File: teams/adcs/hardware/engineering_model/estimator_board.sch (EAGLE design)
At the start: 58 parts, among them U1 Value, U2 Value

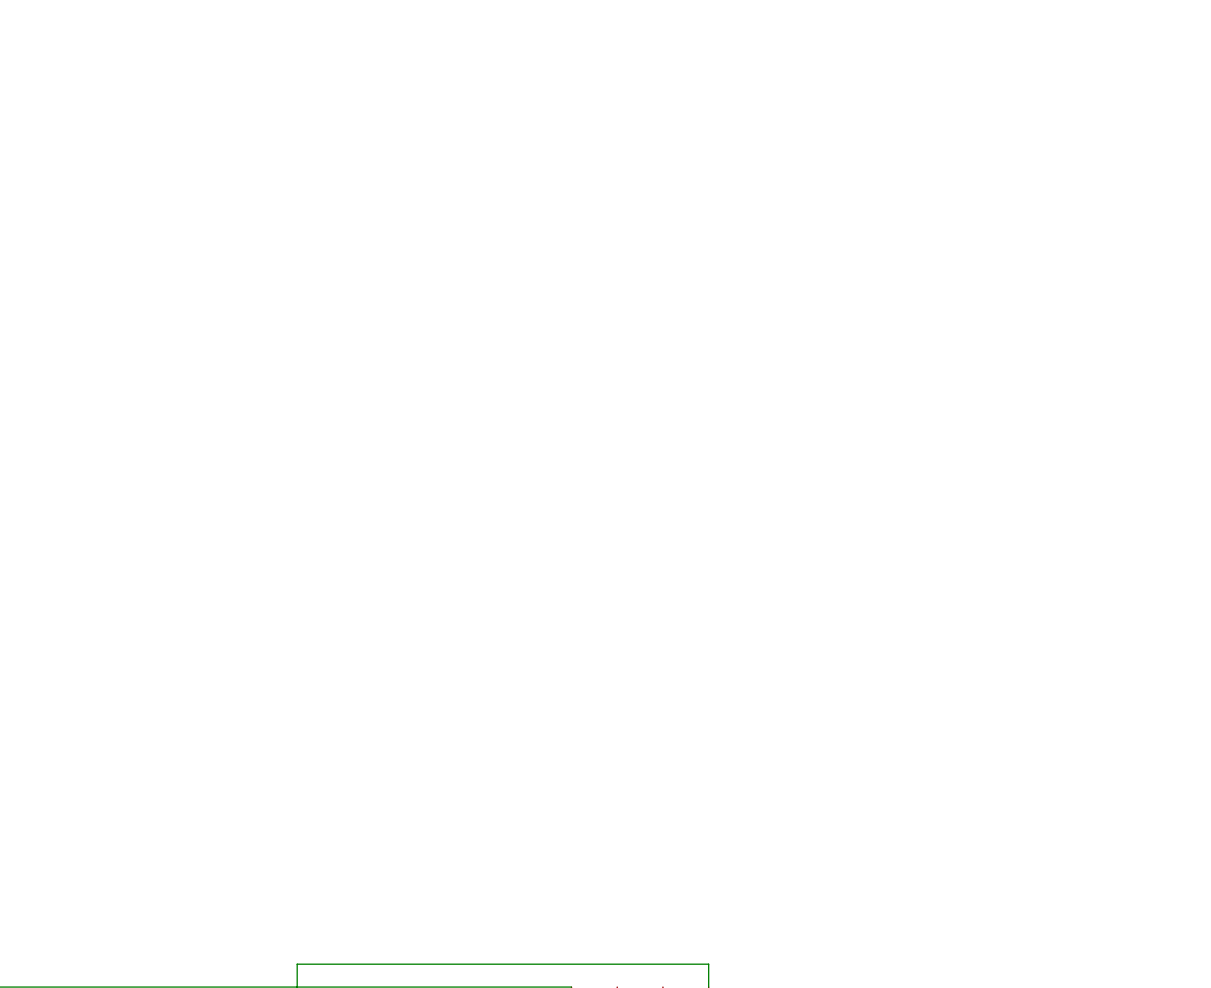
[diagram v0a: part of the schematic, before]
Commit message: ADCS/Estimator: Add LSM6DSM to estimator board (unconnected)
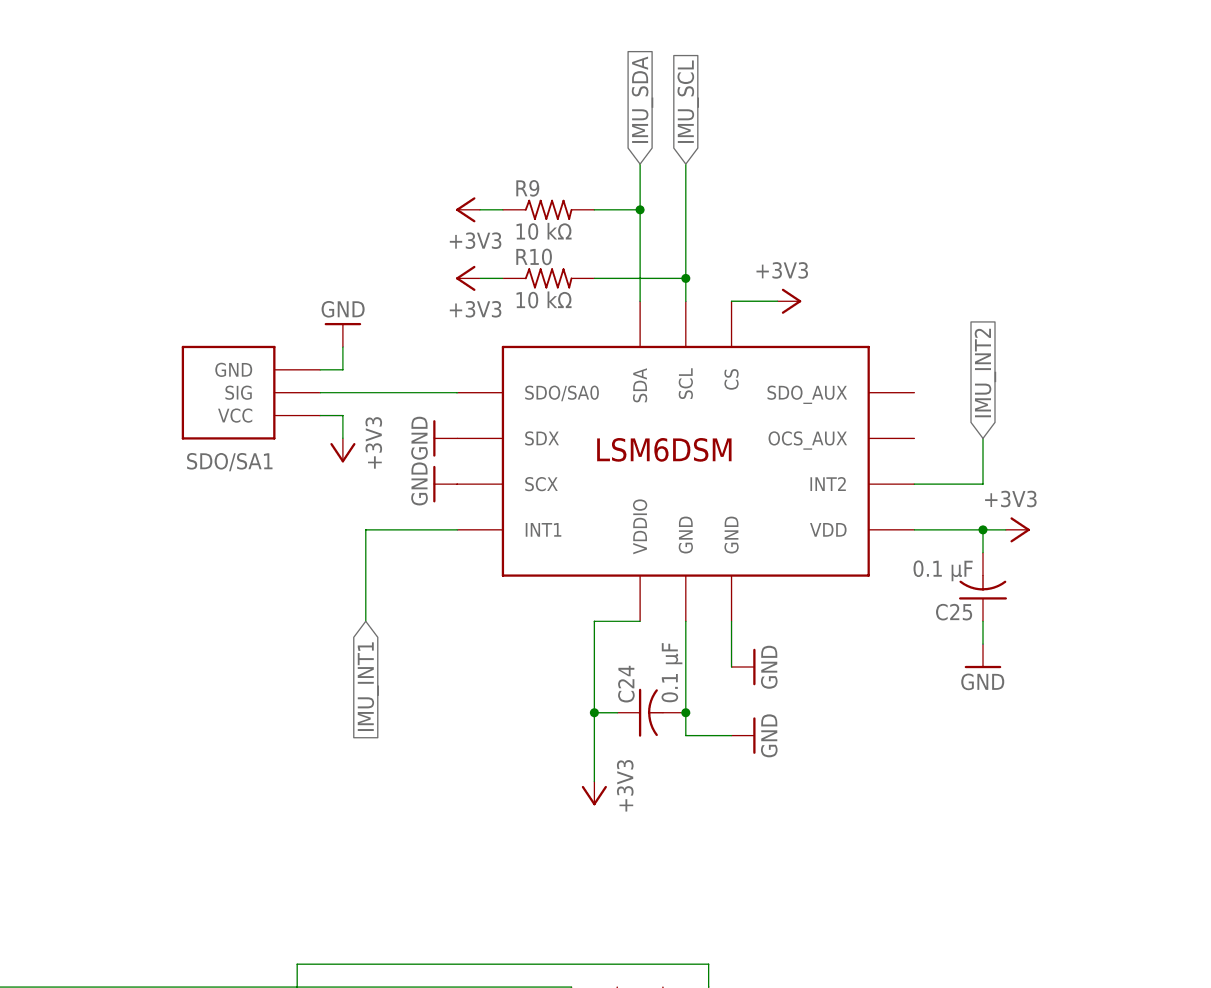
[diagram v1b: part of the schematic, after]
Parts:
- added C24, C25: 0.1 μF, rcl:C-USC0805
- added R10, R9: 10 kΩ, rcl:R-US_M0805
- added SDO/SA1: 0_OHM_JUMPER, DubSat1 Components:0_OHM_JUMPER
- added U$17: LSM6DSM, LSM6DSM:LSM6DSM
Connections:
- new net 3V3: C24.1, C25.2, R10.1, R9.1, SDO/SA1.VCC, U$17.CS, U$17.VDD, U$17.VDDIO
- new net IMU_INT1: U$17.INT1
- new net IMU_INT2: U$17.INT2
- new net IMU_SCL: R10.2, U$17.SCL
- new net IMU_SDA: R9.2, U$17.SDA
- new net N$25: SDO/SA1.SIG, U$17.SDO/SA0
- net GND: now also C24.2, C25.1, SDO/SA1.GND, U$17.GND@1, U$17.GND@2, U$17.SCX, U$17.SDX
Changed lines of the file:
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@@
 <?xml version="1.0" encoding="utf-8"?>
 <!DOCTYPE eagle SYSTEM "eagle.dtd">
-<eagle version="7.5.0">
+<eagle version="8.3.2">
 <drawing>
 <settings>
 <setting alwaysvectorfont="no"/>
+<setting keepoldvectorfont="yes"/>
 <setting verticaltext="up"/>
 </settings>
@@
 <part name="C20" library="DubSat1 Components" deviceset="CAPACITOR" device="0805" value=".1u"/>
 <part name="GND-ISO10" library="SparkFun-Aesthetics" deviceset="GND-ISO" device=""/>
+<part name="U$17" library="LSM6DSM" deviceset="LSM6DSM" device=""/>
+<part name="GND31" library="supply1" library_urn="urn:adsk.eagle:library:371" deviceset="GND" device=""/>
+<part name="GND32" library="supply1" library_urn="urn:adsk.eagle:library:371" deviceset="GND" device=""/>
+<part name="VDD3" library="supply1" library_urn="urn:adsk.eagle:library:371" deviceset="+3V3" device=""/>
+<part name="C24" library="rcl" library_urn="urn:adsk.eagle:library:334" deviceset="C-US" device="C0805" value="0.1 μF"/>
+<part name="VDD8" library="supply1" library_urn="urn:adsk.eagle:library:371" deviceset="+3V3" device=""/>
+<part name="C25" library="rcl" library_urn="urn:adsk.eagle:library:334" deviceset="C-US" device="C0805" value="0.1 μF"/>
+<part name="GND33" library="supply1" library_urn="urn:adsk.eagle:library:371" deviceset="GND" device=""/>
+<part name="GND34" library="supply1" library_urn="urn:adsk.eagle:library:371" deviceset="GND" device=""/>
+<part name="GND35" library="supply1" library_urn="urn:adsk.eagle:library:371" deviceset="GND" device=""/>
+<part name="VDD9" library="supply1" library_urn="urn:adsk.eagle:library:371" deviceset="+3V3" device=""/>
+<part name="R9" library="rcl" library_urn="urn:adsk.eagle:library:334" deviceset="R-US_" device="M0805" value="10 kΩ"/>
+<part name="R10" library="rcl" library_urn="urn:adsk.eagle:library:334" deviceset="R-US_" device="M0805" value="10 kΩ"/>
+<part name="VDD10" library="supply1" library_urn="urn:adsk.eagle:library:371" deviceset="+3V3" device=""/>
+<part name="VDD11" library="supply1" library_urn="urn:adsk.eagle:library:371" deviceset="+3V3" device=""/>
+<part name="SDO/SA1" library="DubSat1 Components" deviceset="0_OHM_JUMPER" device=""/>
+<part name="GND36" library="supply1" library_urn="urn:adsk.eagle:library:371" deviceset="GND" device=""/>
+<part name="VDD12" library="supply1" library_urn="urn:adsk.eagle:library:371" deviceset="+3V3" device=""/>
 </parts>
 <sheets>
@@
 <instance part="C20" gate="G$1" x="195.58" y="215.9"/>
 <instance part="GND-ISO10" gate="G$1" x="198.12" y="210.82"/>
+<instance part="U$17" gate="G$1" x="261.62" y="287.02"/>
+<instance part="GND31" gate="1" x="269.24" y="264.16" rot="R90"/>
+<instance part="GND32" gate="1" x="269.24" y="256.54" rot="R90"/>
+<instance part="VDD3" gate="G$1" x="251.46" y="248.92" rot="R180"/>
+<instance part="C24" gate="G$1" x="256.54" y="259.08" rot="R90"/>
+<instance part="VDD8" gate="G$1" x="299.72" y="279.4" rot="R270"/>
+<instance part="C25" gate="G$1" x="294.64" y="271.78" rot="R180"/>
+<instance part="GND33" gate="1" x="294.64" y="264.16"/>
+<instance part="GND34" gate="1" x="233.68" y="289.56" rot="R270"/>
+<instance part="GND35" gate="1" x="233.68" y="284.48" rot="R270"/>
+<instance part="VDD9" gate="G$1" x="274.32" y="304.8" rot="R270"/>
+<instance part="R9" gate="G$1" x="246.38" y="314.96"/>
+<instance part="R10" gate="G$1" x="246.38" y="307.34"/>
+<instance part="VDD10" gate="G$1" x="236.22" y="314.96" rot="R90"/>
+<instance part="VDD11" gate="G$1" x="236.22" y="307.34" rot="R90"/>
+<instance part="SDO/SA1" gate="G$1" x="205.74" y="292.1" rot="R180"/>
+<instance part="GND36" gate="1" x="223.52" y="302.26" rot="R180"/>
+<instance part="VDD12" gate="G$1" x="223.52" y="287.02" rot="R180"/>
 </instances>
 <busses>
@@
 <pinref part="C15" gate="G$1" pin="2"/>
 <wire x1="-147.32" y1="182.88" x2="-147.32" y2="185.42" width="0.1524" layer="91"/>
+</segment>
+<segment>
+<pinref part="U$17" gate="G$1" pin="GND@2"/>
+<pinref part="GND31" gate="1" pin="GND"/>
+<wire x1="266.7" y1="264.16" x2="266.7" y2="269.24" width="0.1524" layer="91"/>
+</segment>
+<segment>
+<pinref part="U$17" gate="G$1" pin="GND@1"/>
+<pinref part="GND32" gate="1" pin="GND"/>
+<wire x1="261.62" y1="269.24" x2="261.62" y2="259.08" width="0.1524" layer="91"/>
+<wire x1="261.62" y1="259.08" x2="261.62" y2="256.54" width="0.1524" layer="91"/>
+<wire x1="261.62" y1="256.54" x2="266.7" y2="256.54" width="0.1524" layer="91"/>
+<pinref part="C24" gate="G$1" pin="2"/>
+<junction x="261.62" y="259.08"/>
+</segment>
+<segment>
+<pinref part="C25" gate="G$1" pin="1"/>
+<pinref part="GND33" gate="1" pin="GND"/>
+<wire x1="294.64" y1="266.7" x2="294.64" y2="269.24" width="0.1524" layer="91"/>
+</segment>
+<segment>
+<pinref part="U$17" gate="G$1" pin="SDX"/>
+<pinref part="GND34" gate="1" pin="GND"/>
+</segment>
+<segment>
+<pinref part="U$17" gate="G$1" pin="SCX"/>
+<pinref part="GND35" gate="1" pin="GND"/>
+</segment>
+<segment>
+<pinref part="GND36" gate="1" pin="GND"/>
+<pinref part="SDO/SA1" gate="G$1" pin="GND"/>
+<wire x1="223.52" y1="299.72" x2="223.52" y2="297.18" width="0.1524" layer="91"/>
+<wire x1="223.52" y1="297.18" x2="220.98" y2="297.18" width="0.1524" layer="91"/>
 </segment>
 </net>
@@
 </segment>
 </net>
+<net name="3V3" class="0">
+<segment>
+<pinref part="U$17" gate="G$1" pin="VDDIO"/>
+<wire x1="256.54" y1="269.24" x2="251.46" y2="269.24" width="0.1524" layer="91"/>
+<wire x1="251.46" y1="269.24" x2="251.46" y2="259.08" width="0.1524" layer="91"/>
+<pinref part="C24" gate="G$1" pin="1"/>
+<wire x1="251.46" y1="259.08" x2="254" y2="259.08" width="0.1524" layer="91"/>
+<pinref part="VDD3" gate="G$1" pin="+3V3"/>
+<wire x1="251.46" y1="259.08" x2="251.46" y2="251.46" width="0.1524" layer="91"/>
+<junction x="251.46" y="259.08"/>
+</segment>
+<segment>
+<pinref part="U$17" gate="G$1" pin="VDD"/>
+<pinref part="VDD8" gate="G$1" pin="+3V3"/>
+<wire x1="287.02" y1="279.4" x2="294.64" y2="279.4" width="0.1524" layer="91"/>
+<pinref part="C25" gate="G$1" pin="2"/>
+<wire x1="294.64" y1="279.4" x2="297.18" y2="279.4" width="0.1524" layer="91"/>
+<wire x1="294.64" y1="276.86" x2="294.64" y2="279.4" width="0.1524" layer="91"/>
+<junction x="294.64" y="279.4"/>
+</segment>
+<segment>
+<pinref part="U$17" gate="G$1" pin="CS"/>
+<pinref part="VDD9" gate="G$1" pin="+3V3"/>
+<wire x1="266.7" y1="304.8" x2="271.78" y2="304.8" width="0.1524" layer="91"/>
+</segment>
+<segment>
+<pinref part="R9" gate="G$1" pin="1"/>
+<pinref part="VDD10" gate="G$1" pin="+3V3"/>
+<wire x1="241.3" y1="314.96" x2="238.76" y2="314.96" width="0.1524" layer="91"/>
+</segment>
+<segment>
+<pinref part="VDD11" gate="G$1" pin="+3V3"/>
+<pinref part="R10" gate="G$1" pin="1"/>
+<wire x1="238.76" y1="307.34" x2="241.3" y2="307.34" width="0.1524" layer="91"/>
+</segment>
+<segment>
+<pinref part="SDO/SA1" gate="G$1" pin="VCC"/>
+<pinref part="VDD12" gate="G$1" pin="+3V3"/>
+<wire x1="220.98" y1="292.1" x2="223.52" y2="292.1" width="0.1524" layer="91"/>
+<wire x1="223.52" y1="292.1" x2="223.52" y2="289.56" width="0.1524" layer="91"/>
+</segment>
+</net>
+<net name="IMU_SDA" class="0">
+<segment>
+<pinref part="U$17" gate="G$1" pin="SDA"/>
+<wire x1="256.54" y1="304.8" x2="256.54" y2="314.96" width="0.1524" layer="91"/>
+<wire x1="256.54" y1="314.96" x2="256.54" y2="320.04" width="0.1524" layer="91"/>
+<wire x1="256.54" y1="314.96" x2="251.46" y2="314.96" width="0.1524" layer="91"/>
+<pinref part="R9" gate="G$1" pin="2"/>
+<junction x="256.54" y="314.96"/>
+<label x="256.54" y="320.04" size="1.778" layer="95" rot="R90" xref="yes"/>
+</segment>
+</net>
+<net name="IMU_SCL" class="0">
+<segment>
+<pinref part="U$17" gate="G$1" pin="SCL"/>
+<wire x1="261.62" y1="304.8" x2="261.62" y2="307.34" width="0.1524" layer="91"/>
+<wire x1="261.62" y1="307.34" x2="261.62" y2="320.04" width="0.1524" layer="91"/>
+<wire x1="261.62" y1="307.34" x2="251.46" y2="307.34" width="0.1524" layer="91"/>
+<pinref part="R10" gate="G$1" pin="2"/>
+<junction x="261.62" y="307.34"/>
+<label x="261.62" y="320.04" size="1.778" layer="95" rot="R90" xref="yes"/>
+</segment>
+</net>
+<net name="IMU_INT1" class="0">
+<segment>
+<pinref part="U$17" gate="G$1" pin="INT1"/>
+<wire x1="236.22" y1="279.4" x2="226.06" y2="279.4" width="0.1524" layer="91"/>
+<wire x1="226.06" y1="279.4" x2="226.06" y2="269.24" width="0.1524" layer="91"/>
+<label x="226.06" y="269.24" size="1.778" layer="95" rot="R270" xref="yes"/>
+</segment>
+</net>
+<net name="IMU_INT2" class="0">
+<segment>
+<pinref part="U$17" gate="G$1" pin="INT2"/>
+<wire x1="287.02" y1="284.48" x2="294.64" y2="284.48" width="0.1524" layer="91"/>
+<wire x1="294.64" y1="284.48" x2="294.64" y2="289.56" width="0.1524" layer="91"/>
+<label x="294.64" y="289.56" size="1.778" layer="95" rot="R90" xref="yes"/>
+</segment>
+</net>
+<net name="N$25" class="0">
+<segment>
+<pinref part="U$17" gate="G$1" pin="SDO/SA0"/>
+<wire x1="236.22" y1="294.64" x2="220.98" y2="294.64" width="0.1524" layer="91"/>
+<pinref part="SDO/SA1" gate="G$1" pin="SIG"/>
+</segment>
+</net>
 </nets>
 </sheet>
@@
 which will not be processed correctly with this version.
 </note>
+<note version="8.2" severity="warning">
+Since Version 8.2, EAGLE supports online libraries. The ids
+of those online libraries will not be understood (or retained)
+with this version.
+</note>
+<note version="8.3" severity="warning">
+Since Version 8.3, EAGLE supports URNs for individual library
+assets (packages, symbols, and devices). The URNs of those assets
+will not be understood (or retained) with this version.
+</note>
 </compatibility>

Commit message: finished estimator_board
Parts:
- removed L1: (no value), SparkFun-Passives:INDUCTOR0805
- removed R4: 2.2KΩ, DubSat1 Components:RESISTOR0805
- added C22: 0.22µF, DubSat1 Components:CAPACITOR0805
- added C23, C28: .1u, DubSat1 Components:CAPACITOR0805
- added C26: 4.7u, DubSat1 Components:CAPACITOR0805
- added C27: 1u, DubSat1 Components:CAPACITOR0805
- added JP1, JP10, JP2, JP3, JP4, JP5, JP6, JP7, JP8, JP9: M02PTH, SparkFun-Connectors:M02PTH
- added R7: 2.2KΩ, DubSat1 Components:RESISTOR0805
- added U$18: HMC5983, DubSat1 Components:HMC5983
- R10, R9: value 10 kΩ -> 2.2KΩ; device rcl:R-US_M0805 -> DubSat1 Components:RESISTOR0805
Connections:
- removed net 3V3: C24.1, C25.2, R10.1, R9.1, SDO/SA1.VCC, U$17.CS, U$17.VDD, U$17.VDDIO
- removed net IMU_SCL: R10.2, U$17.SCL
- removed net IMU_SDA: R9.2, U$17.SDA
- removed net N$23: C21.1, L1.2, R3.1, R4.1, U$15.!SPI_CS, U$15.I2C/!SPI, U$15.VDD, U$15.VDDIO
- new net N$22: JP10.2, U$15.DRDY
- new net N$26: JP3.2, U$18.SCL/SPI_SCK
- new net N$27: JP6.1, R7.2, U$7.P5.1_I2C-SCL-1
- new net N$28: JP5.2, R3.2, U$7.P5.0_I2C-SDA-1
- new net N$29: JP8.2, U2A.P4.6_A7
- new net N$30: JP7.1, U2A.P4.5_A8
- new net N$31: JP10.1, U$7.P1.7_GPIO/PWM
- new net N$32: JP9.2, U2A.P4.7_A6
- new net N$34: C26.1, U$18.C1
- new net N$35: C22.2, U$18.SETP
- new net N$36: C22.1, U$18.SETC
- new net N$38: JP7.2, U$18.DRDY
- net 3.3V: now also C23.1, C24.1, C25.2, C27.1, C28.1, R10.1, R9.1, SDO/SA1.VCC, U$17.CS, U$17.VDD, U$17.VDDIO, U$18.!SPI_CS, U$18.I2C/!SPI, U$18.VDD, U$18.VDDIO
- net 3.3V-ISO: now also C21.1, R3.1, R7.1, U$15.!SPI_CS, U$15.I2C/!SPI, U$15.VDD, U$15.VDDIO; no longer L1.1
- net GND: now also C23.2, C26.2, C27.2, C28.2, U$18.GND, U$18.SOC
- net I2C_SCL2: now also JP2.1, JP2.2, JP3.1, R10.2, U$17.SCL
- net I2C_SDA2: now also JP1.1, JP1.2, JP4.1, JP4.2, R9.2, U$17.SDA, U$18.SDA/SPI_SDI
- net IMU_INT1: now also JP9.1
- net IMU_INT2: now also JP8.1
- net N$16: now also JP5.1; no longer R4.2, U$7.P5.0_I2C-SDA-1
- net N$18: now also JP6.2; no longer R3.2, U$7.P5.1_I2C-SCL-1
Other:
- moved on the sheet: C17, C18, C19, C20, C21, C24, C25, R10, R3, R9, SDO/SA1
